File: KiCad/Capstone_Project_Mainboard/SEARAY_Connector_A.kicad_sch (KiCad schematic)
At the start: 1 part, among them J1 ASP-134486

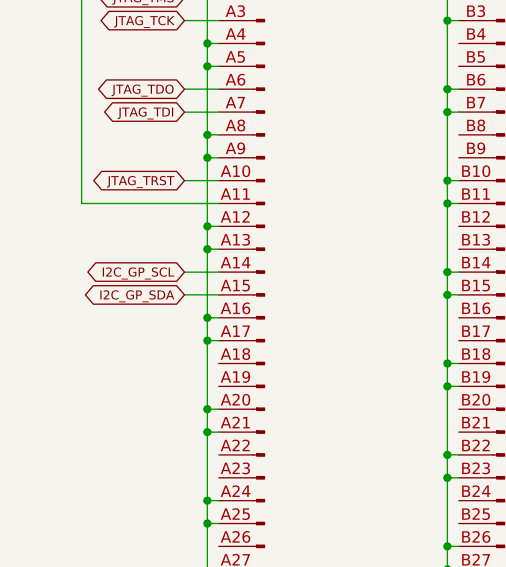
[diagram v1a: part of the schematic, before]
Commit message: Core non-power parts defined
Most major non-power components added to KiCad project
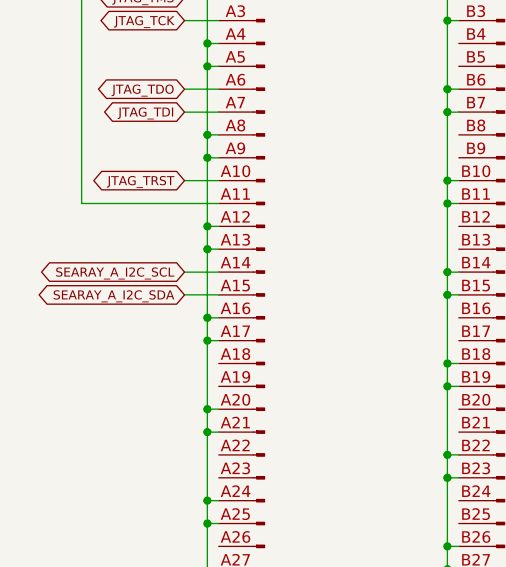
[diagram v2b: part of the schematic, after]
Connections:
- net I2C_GP_SCL renamed SEARAY_A_I2C_SCL
- net I2C_GP_SDA renamed SEARAY_A_I2C_SDA
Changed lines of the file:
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@@
   (title_block
     (title "10x40 SEARAY Connector A")
-    (date "2023-12-22")
+    (date "2023-12-26")
     (rev "A")
     (company "Jordan Harris-Toovy")
@@
     )
   )
-  (global_label "I2C_GP_SDA" (shape bidirectional) (at 33.02 72.39 180) (fields_autoplaced)
+  (global_label "SEARAY_A_I2C_SDA" (shape bidirectional) (at 33.02 72.39 180) (fields_autoplaced)
     (effects (font (size 1 1) (color 65 65 65 1)) (justify right))
-    (property "Intersheetrefs" "${INTERSHEET_REFS}" (at 33.02 72.39 0)
-      (effects (font (size 1.27 1.27)) hide)
+    (property "Intersheetrefs" "${INTERSHEET_REFS}" (at 15.9853 72.39 0)
+      (effects (font (size 1.27 1.27)) (justify right) hide)
     )
   )
@@
     )
   )
-  (global_label "I2C_GP_SCL" (shape bidirectional) (at 33.02 69.85 180) (fields_autoplaced)
+  (global_label "SEARAY_A_I2C_SCL" (shape bidirectional) (at 33.02 69.85 180) (fields_autoplaced)
     (effects (font (size 1 1) (color 65 65 65 1)) (justify right))
-    (property "Intersheetrefs" "${INTERSHEET_REFS}" (at 33.02 69.85 0)
-      (effects (font (size 1.27 1.27)) hide)
+    (property "Intersheetrefs" "${INTERSHEET_REFS}" (at 16.0329 69.85 0)
+      (effects (font (size 1.27 1.27)) (justify right) hide)
     )
   )
